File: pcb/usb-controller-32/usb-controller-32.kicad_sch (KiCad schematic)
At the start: 3 parts, among them U1 PIC32MX250F128B, U2 MAX3232, U3 MCP23017x-x-SP

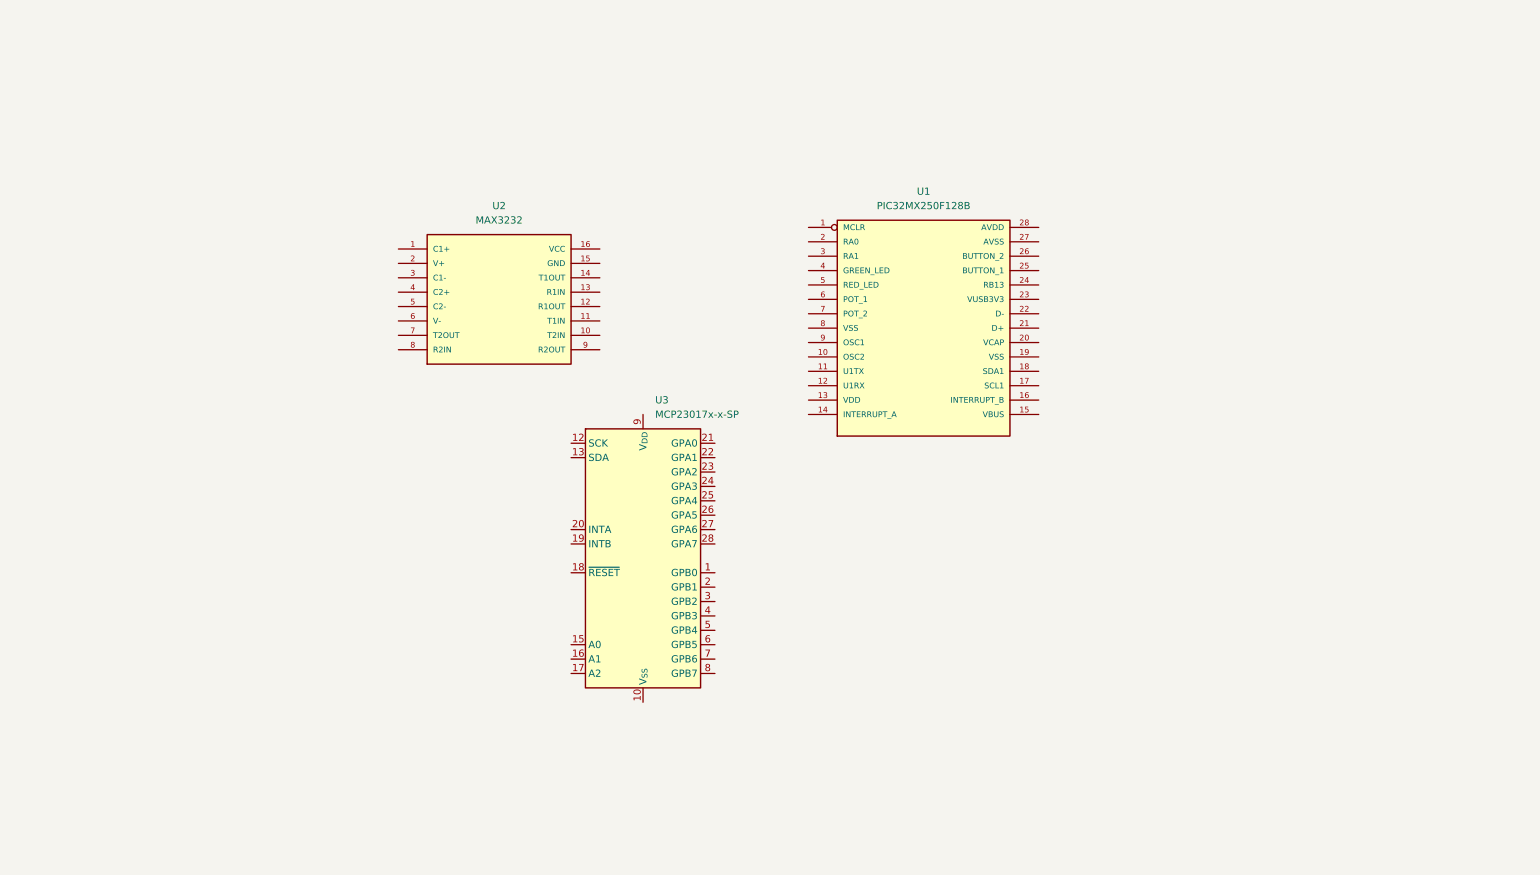
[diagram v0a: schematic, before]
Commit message: update adafruit breakout footprint and model
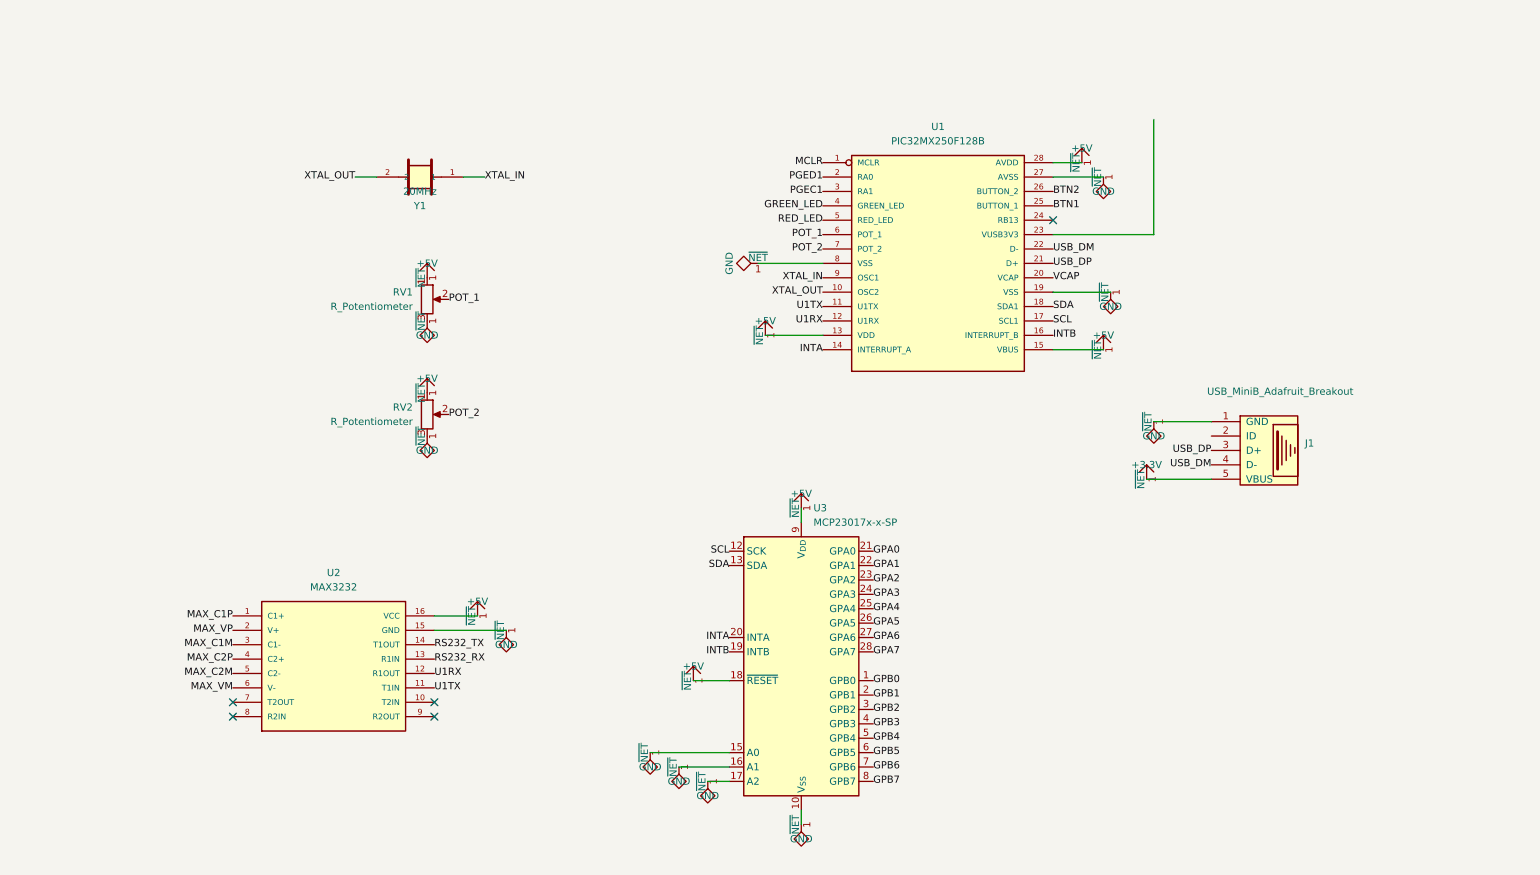
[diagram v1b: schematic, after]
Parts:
- added J1: USB_MiniB_Adafruit_Breakout, extra:USB_MiniB_Adafruit_Breakout, symbol extra:USB_MiniB_Adafruit_Breakout
- added RV1, RV2: R_Potentiometer, Potentiometer_THT:Potentiometer_Bourns_3005_Horizontal, symbol Device:R_Potentiometer
- added Y1: 20MHz, extra:Crystal_HC49-U_Vertical_20MHz, symbol extra:XTAL_20MHz
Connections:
- net GPB0: now reaches U3.1 (GPB0)
- net GND: now reaches U3.10 (V_{SS})
- net GND: now also U1.19 (VSS), U1.27 (AVSS), U1.8 (VSS), U2.15 (GND), U3.15 (A0), U3.16 (A1), U3.17 (A2), J1.1 (GND), RV1.3, RV2.3
- net SCL: now reaches U3.12 (SCK)
- net SCL: now also U1.17 (SCL1)
- net SDA: now reaches U3.13 (SDA)
- net SDA: now also U1.18 (SDA1)
- net +5V: now reaches U3.18 (~{RESET})
- net +5V: now also U1.13 (VDD), U1.15 (VBUS), U1.28 (AVDD), U2.16 (VCC), U3.9 (V_{DD}), RV1.1, RV2.1
- net INTB: now reaches U3.19 (INTB)
- net INTB: now also U1.16 (INTERRUPT_B)
- net GPB1: now reaches U3.2 (GPB1)
- net INTA: now reaches U3.20 (INTA)
- net INTA: now also U1.14 (INTERRUPT_A)
- net GPA0: now reaches U3.21 (GPA0)
- net GPA1: now reaches U3.22 (GPA1)
- net GPA2: now reaches U3.23 (GPA2)
- net GPA3: now reaches U3.24 (GPA3)
- net GPA4: now reaches U3.25 (GPA4)
- net GPA5: now reaches U3.26 (GPA5)
- net GPA6: now reaches U3.27 (GPA6)
- net GPA7: now reaches U3.28 (GPA7)
- net GPB2: now reaches U3.3 (GPB2)
- net GPB3: now reaches U3.4 (GPB3)
- net GPB4: now reaches U3.5 (GPB4)
- net GPB5: now reaches U3.6 (GPB5)
- net GPB6: now reaches U3.7 (GPB6)
- net GPB7: now reaches U3.8 (GPB7)
- net MAX_C1P: now reaches U2.1 (C1+)
- net U1TX: now reaches U2.11 (T1IN)
- net U1TX: now also U1.11 (U1TX)
- net U1RX: now reaches U2.12 (R1OUT)
- net U1RX: now also U1.12 (U1RX)
- net RS232_RX: now reaches U2.13 (R1IN)
- net RS232_TX: now reaches U2.14 (T1OUT)
- net MAX_VP: now reaches U2.2 (V+)
- net MAX_C1M: now reaches U2.3 (C1-)
- net MAX_C2P: now reaches U2.4 (C2+)
- net MAX_C2M: now reaches U2.5 (C2-)
- net MAX_VM: now reaches U2.6 (V-)
- net MCLR: now reaches U1.1 (MCLR)
- net XTAL_OUT: now reaches U1.10 (OSC2)
- net XTAL_OUT: now also Y1.2
- net PGED1: now reaches U1.2 (RA0)
- net VCAP: now reaches U1.20 (VCAP)
- net USB_DP: now reaches U1.21 (D+)
- net USB_DP: now also J1.3 (D+)
- net USB_DM: now reaches U1.22 (D-)
- net USB_DM: now also J1.4 (D-)
- net BTN1: now reaches U1.25 (BUTTON_1)
- net BTN2: now reaches U1.26 (BUTTON_2)
- net PGEC1: now reaches U1.3 (RA1)
- net GREEN_LED: now reaches U1.4 (GREEN_LED)
- net RED_LED: now reaches U1.5 (RED_LED)
- net POT_1: now reaches U1.6 (POT_1)
- net POT_1: now also RV1.2
- net POT_2: now reaches U1.7 (POT_2)
- net POT_2: now also RV2.2
- net XTAL_IN: now reaches U1.9 (OSC1)
- net XTAL_IN: now also Y1.1
- new net +3.3V: J1.5 (VBUS)
- no-connect marks 0 -> 5
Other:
- moved on the sheet: U1, U2, U3

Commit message: - finish schematic - add BOM
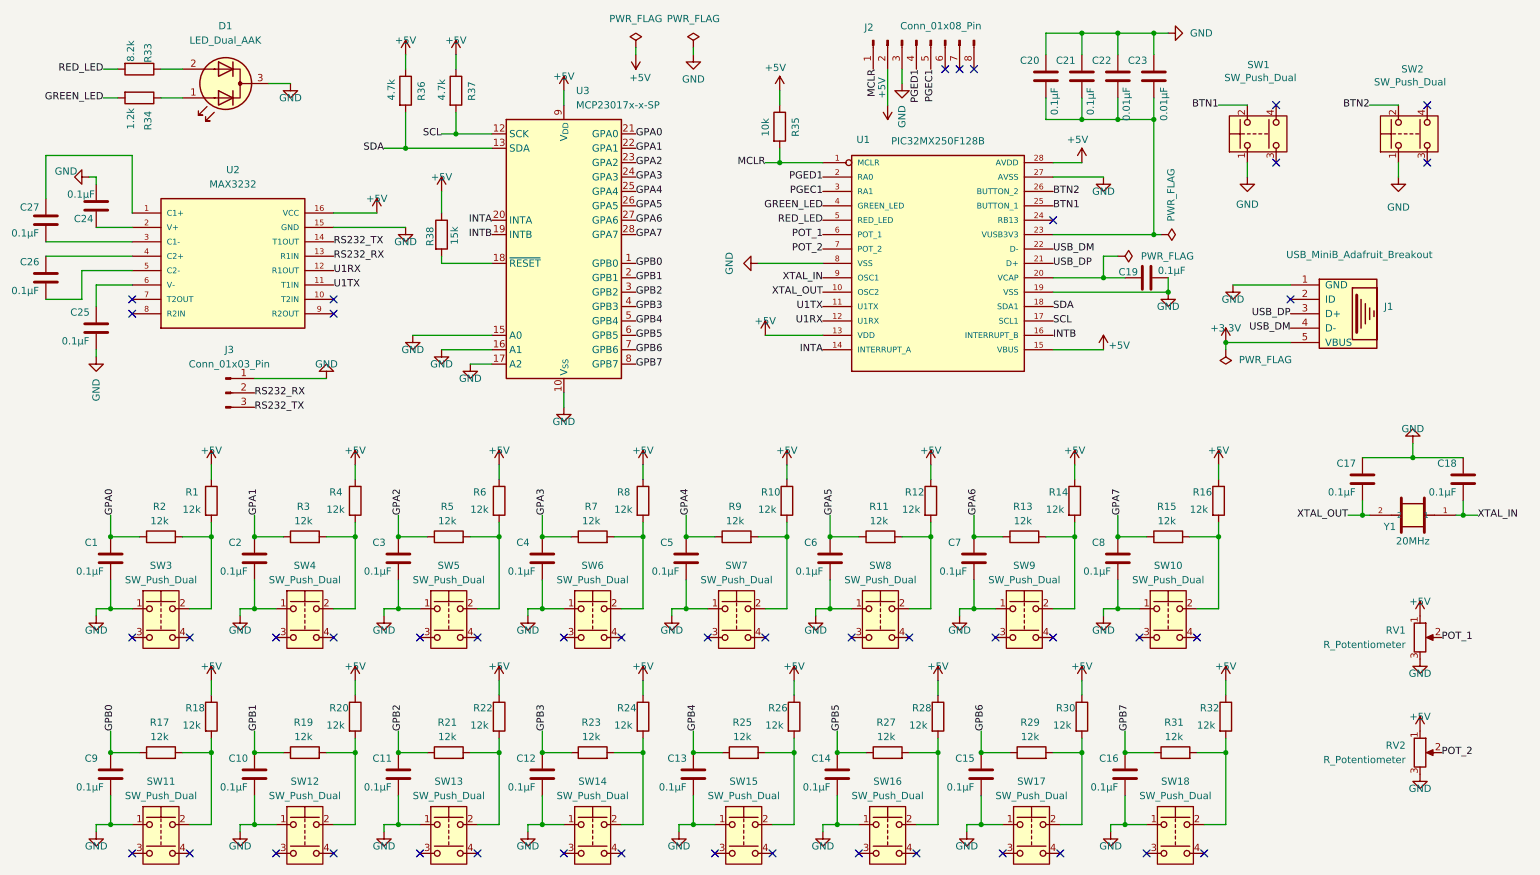
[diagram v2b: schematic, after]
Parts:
- added C1, C10, C11, C12, C13, C14, C15, C16, C17, C18, C19, C2, C20, C21, C24, C25, C26, C27, C3, C4, C5, C6, C7, C8, C9: 0.1µF, Capacitor_THT:C_Disc_D5.0mm_W2.5mm_P2.50mm, symbol Device:C
- added C22, C23: 0.01µF, Capacitor_THT:C_Disc_D5.0mm_W2.5mm_P2.50mm, symbol Device:C
- added D1: LED_Dual_AAK, LED_THT:LED_D5.0mm-3, symbol Device:LED_Dual_AAK
- added J2: Conn_01x08_Pin, Connector_PinHeader_2.54mm:PinHeader_1x08_P2.54mm_Vertical, symbol Connector:Conn_01x08_Pin
- added J3: Conn_01x03_Pin, Connector_PinHeader_2.54mm:PinHeader_1x03_P2.54mm_Vertical, symbol Connector:Conn_01x03_Pin
- added R1, R10, R11, R12, R13, R14, R15, R16, R17, R18, R19, R2, R20, R21, R22, R23, R24, R25, R26, R27, R28, R29, R3, R30, R31, R32, R4, R5, R6, R7, R8, R9: 12k, Resistor_THT:R_Axial_DIN0207_L6.3mm_D2.5mm_P10.16mm_Horizontal, symbol Device:R
- added R33: 8.2k, Resistor_THT:R_Axial_DIN0207_L6.3mm_D2.5mm_P10.16mm_Horizontal, symbol Device:R
- added R34: 1.2k, Resistor_THT:R_Axial_DIN0207_L6.3mm_D2.5mm_P10.16mm_Horizontal, symbol Device:R
- added R35: 10k, Resistor_THT:R_Axial_DIN0207_L6.3mm_D2.5mm_P10.16mm_Horizontal, symbol Device:R
- added R36, R37: 4.7k, Resistor_THT:R_Axial_DIN0207_L6.3mm_D2.5mm_P10.16mm_Horizontal, symbol Device:R
- added R38: 15k, Resistor_THT:R_Axial_DIN0207_L6.3mm_D2.5mm_P10.16mm_Horizontal, symbol Device:R
- added SW1, SW10, SW11, SW12, SW13, SW14, SW15, SW16, SW17, SW18, SW2, SW3, SW4, SW5, SW6, SW7, SW8, SW9: SW_Push_Dual, Button_Switch_THT:SW_TH_Tactile_Omron_B3F-100x, symbol Switch:SW_Push_Dual
- RV1, RV2: footprint Potentiometer_THT:Potentiometer_Bourns_3005_Horizontal -> Potentiometer_THT:Potentiometer_Bourns_3386P_Vertical
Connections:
- net +5V: now also J2.2 (Pin_2), R1.1, R10.1, R12.1, R14.1, R16.1, R18.1, R20.1, R22.1, R24.1, R26.1, R28.1, R30.1, R32.1, R35.1, R36.1, R37.1, R38.1, R4.1, R6.1, R8.1; no longer U3.18 (~{RESET})
- net BTN1: now also SW1.2
- net BTN2: now also SW2.2
- net GND: now also C1.1, C10.1, C11.1, C12.1, C13.1, C14.1, C15.1, C16.1, C17.2, C18.2, C19.1, C2.1, C20.2, C21.2, C22.2, C23.2, C24.1, C25.1, C3.1, C4.1, C5.1, C6.1, C7.1, C8.1, C9.1, D1.3 (K), J2.3 (Pin_3), J3.1 (Pin_1), SW1.1, SW10.1, SW11.1, SW12.1, SW13.1, SW14.1, SW15.1, SW16.1, SW17.1, SW18.1, SW2.1, SW3.1, SW4.1, SW5.1, SW6.1, SW7.1, SW8.1, SW9.1
- net GPA0: now also C1.2, R2.1
- net GPA1: now also C2.2, R3.1
- net GPA2: now also C3.2, R5.1
- net GPA3: now also C4.2, R7.1
- net GPA4: now also C5.2, R9.1
- net GPA5: now also C6.2, R11.1
- net GPA6: now also C7.2, R13.1
- net GPA7: now also C8.2, R15.1
- net GPB0: now also C9.2, R17.1
- net GPB1: now also C10.2, R19.1
- net GPB2: now also C11.2, R21.1
- net GPB3: now also C12.2, R23.1
- net GPB4: now also C13.2, R25.1
- net GPB5: now also C14.2, R27.1
- net GPB6: now also C15.2, R29.1
- net GPB7: now also C16.2, R31.1
- net GREEN_LED: now also R34.2
- net MCLR: now also J2.1 (Pin_1), R35.2
- net PGEC1: now also J2.5 (Pin_5)
- net PGED1: now also J2.4 (Pin_4)
- net RED_LED: now also R33.2
- net RS232_RX: now also J3.2 (Pin_2)
- net RS232_TX: now also J3.3 (Pin_3)
- net SCL: now also R37.2
- net SDA: now also R36.2
- net XTAL_IN: now also C18.1
- net XTAL_OUT: now also C17.1
- net at U1.23 (VUSB3V3): now also C20.1, C21.1, C22.1, C23.1
- net MAX_C1M: no longer names the net of U2.3 (C1-)
- net MAX_C1M: now also C27.1
- net MAX_C1P: no longer names the net of U2.1 (C1+)
- net MAX_C1P: now also C27.2
- net MAX_C2M: no longer names the net of U2.5 (C2-)
- net MAX_C2M: now also C26.1
- net MAX_C2P: no longer names the net of U2.4 (C2+)
- net MAX_C2P: now also C26.2
- net MAX_VM: no longer names the net of U2.6 (V-)
- net MAX_VM: now also C25.2
- net MAX_VP: no longer names the net of U2.2 (V+)
- net MAX_VP: now also C24.2
- net VCAP: no longer names the net of U1.20 (VCAP)
- net VCAP: now also C19.2
- new net: R3.2, R4.2, SW4.2
- new net: R5.2, R6.2, SW5.2
- new net: R38.2, U3.18 (~{RESET})
- new net: R17.2, R18.2, SW11.2
- new net: R21.2, R22.2, SW13.2
- new net: R15.2, R16.2, SW10.2
- new net: R29.2, R30.2, SW17.2
- new net: R27.2, R28.2, SW16.2
- new net: R25.2, R26.2, SW15.2
- new net: D1.2 (A2), R33.1
- new net: R1.2, R2.2, SW3.2
- new net: R10.2, R9.2, SW7.2
- new net: D1.1 (A1), R34.1
- new net: R11.2, R12.2, SW8.2
- new net: R7.2, R8.2, SW6.2
- new net: R13.2, R14.2, SW9.2
- new net: R19.2, R20.2, SW12.2
- new net: R23.2, R24.2, SW14.2
- new net: R31.2, R32.2, SW18.2
- no-connect marks 5 -> 45
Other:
- moved on the sheet: J1, RV1, RV2, U2, U3, Y1

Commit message: use different crystal footprint
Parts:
- Y1: footprint extra:Crystal_HC49-U_Vertical_20MHz -> Crystal:Crystal_HC49-4H_Vertical
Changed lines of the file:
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@@
 			)
 		)
-		(property "Footprint" "extra:Crystal_HC49-U_Vertical_20MHz"
+		(property "Footprint" "Crystal:Crystal_HC49-4H_Vertical"
 			(at 260.35 101.6 0)
 			(hide yes)

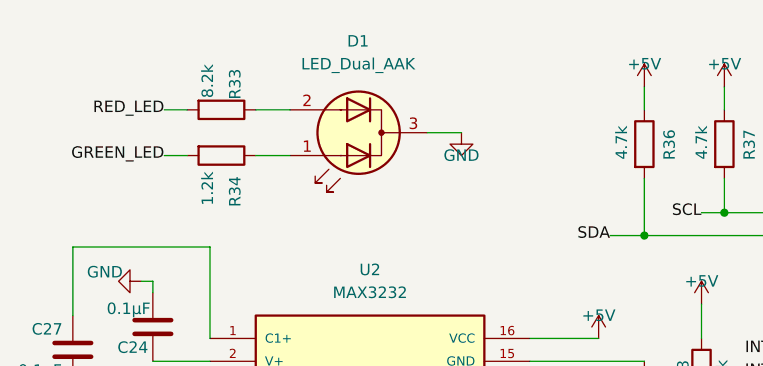
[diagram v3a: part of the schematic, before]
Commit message: update pcb replace led footprint with gnd in middle
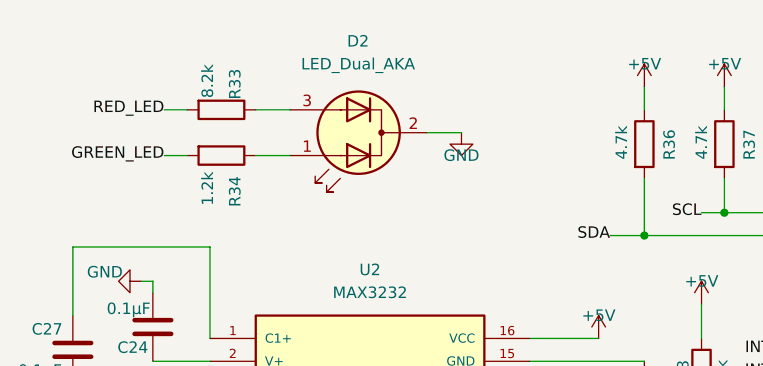
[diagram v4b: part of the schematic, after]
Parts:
- removed D1: LED_Dual_AAK, LED_THT:LED_D5.0mm-3, symbol Device:LED_Dual_AAK
- added D2: LED_Dual_AKA, LED_THT:LED_D3.0mm-3, symbol Device:LED_Dual_AKA
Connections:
- net GND: now also D2.2 (K)
- net at R33.1: now also D2.3 (A2)
- net at R34.1: now also D2.1 (A1)
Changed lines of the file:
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@@
-	)
-	(symbol
-		(lib_id "Device:LED_Dual_AAK")
-		(at 50.8 25.4 180)
-		(unit 1)
-		(body_style 1)
-		(exclude_from_sim no)
-		(in_bom yes)
-		(on_board yes)
-		(in_pos_files yes)
-		(dnp no)
-		(fields_autoplaced yes)
-		(property "Reference" "D1"
-			(at 50.7365 15.24 0)
-			(show_name no)
-			(do_not_autoplace no)
-			(effects
-				(font
-					(size 1.27 1.27)
-				)
-			)
-		)
-		(property "Value" "LED_Dual_AAK"
-			(at 50.7365 17.78 0)
-			(show_name no)
-			(do_not_autoplace no)
-			(effects
-				(font
-					(size 1.27 1.27)
-				)
-			)
-		)
-		(property "Footprint" "LED_THT:LED_D5.0mm-3"
-			(at 50.8 25.4 0)
-			(hide yes)
-			(show_name no)
-			(do_not_autoplace no)
-			(effects
-				(font
-					(size 1.27 1.27)
-				)
-			)
-		)
-		(property "Datasheet" ""
-			(at 50.8 25.4 0)
-			(hide yes)
-			(show_name no)
-			(do_not_autoplace no)
-			(effects
-				(font
-					(size 1.27 1.27)
-				)
-			)
-		)
-		(property "Description" "Dual LED, common cathode on pin 3"
-			(at 50.8 25.4 0)
-			(hide yes)
-			(show_name no)
-			(do_not_autoplace no)
-			(effects
-				(font
-					(size 1.27 1.27)
-				)
-			)
-		)
-		(pin "2"
-		)
-		(pin "3"
-		)
-		(pin "1"
-		)
-		(instances
-			(project "usb-controller-32"
-				(path "/0df98f2e-e784-4feb-8fde-1ac2a09b72c2"
-					(reference "D1")
-					(unit 1)
-				)
-			)
-		)
 	)
 	(symbol
@@
 					(unit 1)
 				)
+			)
+		)
+	)
+	(symbol
+		(lib_id "Device:LED_Dual_AKA")
+		(at 50.8 25.4 180)
+		(unit 1)
+		(body_style 1)
+		(exclude_from_sim no)
+		(in_bom yes)
+		(on_board yes)
+		(in_pos_files yes)
+		(dnp no)
+		(fields_autoplaced yes)
+		(property "Reference" "D2"
+			(at 50.7365 15.24 0)
+			(show_name no)
+			(do_not_autoplace no)
+			(effects
+				(font
+					(size 1.27 1.27)
+				)
+			)
+		)
+		(property "Value" "LED_Dual_AKA"
+			(at 50.7365 17.78 0)
+			(show_name no)
+			(do_not_autoplace no)
+			(effects
+				(font
+					(size 1.27 1.27)
+				)
+			)
+		)
+		(property "Footprint" "LED_THT:LED_D3.0mm-3"
+			(at 50.8 25.4 0)
+			(hide yes)
+			(show_name no)
+			(do_not_autoplace no)
+			(effects
+				(font
+					(size 1.27 1.27)
+				)
+			)
+		)
+		(property "Datasheet" ""
+			(at 50.8 25.4 0)
+			(hide yes)
+			(show_name no)
+			(do_not_autoplace no)
+			(effects
+				(font
+					(size 1.27 1.27)
+				)
+			)
+		)
+		(property "Description" "Dual LED, common cathode on pin 2"
+			(at 50.8 25.4 0)
+			(hide yes)
+			(show_name no)
+			(do_not_autoplace no)
+			(effects
+				(font
+					(size 1.27 1.27)
+				)
+			)
+		)
+		(pin "1"
+		)
+		(pin "2"
+		)
+		(pin "3"
+		)
+		(instances
+			(project "usb-controller-32"
+				(path "/0df98f2e-e784-4feb-8fde-1ac2a09b72c2"
+					(reference "D2")
+					(unit 1)
+				)
